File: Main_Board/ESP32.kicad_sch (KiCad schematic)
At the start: 25 parts, among them J1 RESET, J2 MAIN_UART, Q1 2N7002, U1 W25Q128JVS, U2 ESP32-S3-MINI-1U

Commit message: memory fix + piro
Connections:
- net CLK_SPI2: now also U2.18 (IO14); no longer U2.17 (IO13)
- net IO0 / MOSI: now also U2.17 (IO13); no longer U2.18 (IO14)
- net IO2 / WP: now also U2.16 (IO12); no longer U2.19 (IO15)
- net IO3 / HOLD: no longer U1.7 (~{HOLD}/~{RESET}/IO_{3}), U2.16 (IO12)
- new net: U1.7 (~{HOLD}/~{RESET}/IO_{3}), U2.19 (IO15)
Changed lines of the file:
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@@
+	(wire
+		(pts
+			(xy 105.41 138.43) (xy 111.76 138.43)
+		)
+		(stroke
+			(width 0)
+			(type default)
+		)
+	)
 	(wire
 		(pts
@@
 	(wire
 		(pts
-			(xy 71.12 134.62) (xy 125.73 134.62)
+			(xy 110.49 142.24) (xy 125.73 142.24)
 		)
 		(stroke
@@
 	(wire
 		(pts
-			(xy 71.12 137.16) (xy 125.73 137.16)
+			(xy 71.12 142.24) (xy 109.22 142.24)
 		)
 		(stroke
@@
 	(wire
 		(pts
-			(xy 71.12 142.24) (xy 125.73 142.24)
-		)
-		(stroke
-			(width 0)
-			(type default)
-		)
-	)
-	(wire
-		(pts
 			(xy 71.12 132.08) (xy 125.73 132.08)
 		)
@@
 	(wire
 		(pts
+			(xy 106.68 139.7) (xy 125.73 139.7)
+		)
+		(stroke
+			(width 0)
+			(type default)
+		)
+	)
+	(wire
+		(pts
 			(xy 193.04 93.98) (xy 193.04 101.6)
 		)
@@
 	(wire
 		(pts
+			(xy 111.76 137.16) (xy 125.73 137.16)
+		)
+		(stroke
+			(width 0)
+			(type default)
+		)
+	)
+	(wire
+		(pts
 			(xy 233.68 96.52) (xy 233.68 86.36)
 		)
@@
 	(wire
 		(pts
+			(xy 106.68 137.16) (xy 106.68 139.7)
+		)
+		(stroke
+			(width 0)
+			(type default)
+		)
+	)
+	(wire
+		(pts
 			(xy 200.66 88.9) (xy 201.93 88.9)
 		)
@@
 	(wire
 		(pts
-			(xy 71.12 139.7) (xy 125.73 139.7)
-		)
-		(stroke
-			(width 0)
-			(type default)
-		)
-	)
-	(wire
-		(pts
 			(xy 106.68 116.84) (xy 110.49 116.84)
 		)
@@
 	(wire
 		(pts
+			(xy 109.22 134.62) (xy 125.73 134.62)
+		)
+		(stroke
+			(width 0)
+			(type default)
+		)
+	)
+	(wire
+		(pts
 			(xy 119.38 147.32) (xy 125.73 147.32)
 		)
@@
 	(wire
 		(pts
+			(xy 110.49 140.97) (xy 110.49 142.24)
+		)
+		(stroke
+			(width 0)
+			(type default)
+		)
+	)
+	(wire
+		(pts
 			(xy 114.3 99.06) (xy 125.73 99.06)
 		)
@@
 	(wire
 		(pts
+			(xy 83.82 140.97) (xy 110.49 140.97)
+		)
+		(stroke
+			(width 0)
+			(type default)
+		)
+	)
+	(wire
+		(pts
 			(xy 104.14 149.86) (xy 111.76 149.86)
 		)
@@
 	(wire
 		(pts
+			(xy 83.82 134.62) (xy 83.82 140.97)
+		)
+		(stroke
+			(width 0)
+			(type default)
+		)
+	)
+	(wire
+		(pts
+			(xy 71.12 134.62) (xy 83.82 134.62)
+		)
+		(stroke
+			(width 0)
+			(type default)
+		)
+	)
+	(wire
+		(pts
 			(xy 104.14 147.32) (xy 111.76 147.32)
 		)
@@
 	(wire
 		(pts
+			(xy 111.76 137.16) (xy 111.76 138.43)
+		)
+		(stroke
+			(width 0)
+			(type default)
+		)
+	)
+	(wire
+		(pts
 			(xy 54.61 34.29) (xy 54.61 33.02)
 		)
@@
 	(wire
 		(pts
+			(xy 71.12 139.7) (xy 105.41 139.7)
+		)
+		(stroke
+			(width 0)
+			(type default)
+		)
+	)
+	(wire
+		(pts
 			(xy 106.68 119.38) (xy 110.49 119.38)
 		)
@@
 	(wire
 		(pts
+			(xy 105.41 138.43) (xy 105.41 139.7)
+		)
+		(stroke
+			(width 0)
+			(type default)
+		)
+	)
+	(wire
+		(pts
+			(xy 109.22 142.24) (xy 109.22 134.62)
+		)
+		(stroke
+			(width 0)
+			(type default)
+		)
+	)
+	(wire
+		(pts
 			(xy 60.96 123.19) (xy 60.96 124.46)
 		)
@@
 		)
 		(stroke
+			(width 0)
+			(type default)
+		)
+	)
+	(wire
+		(pts
+			(xy 71.12 137.16) (xy 106.68 137.16)
+		)
+		(stroke

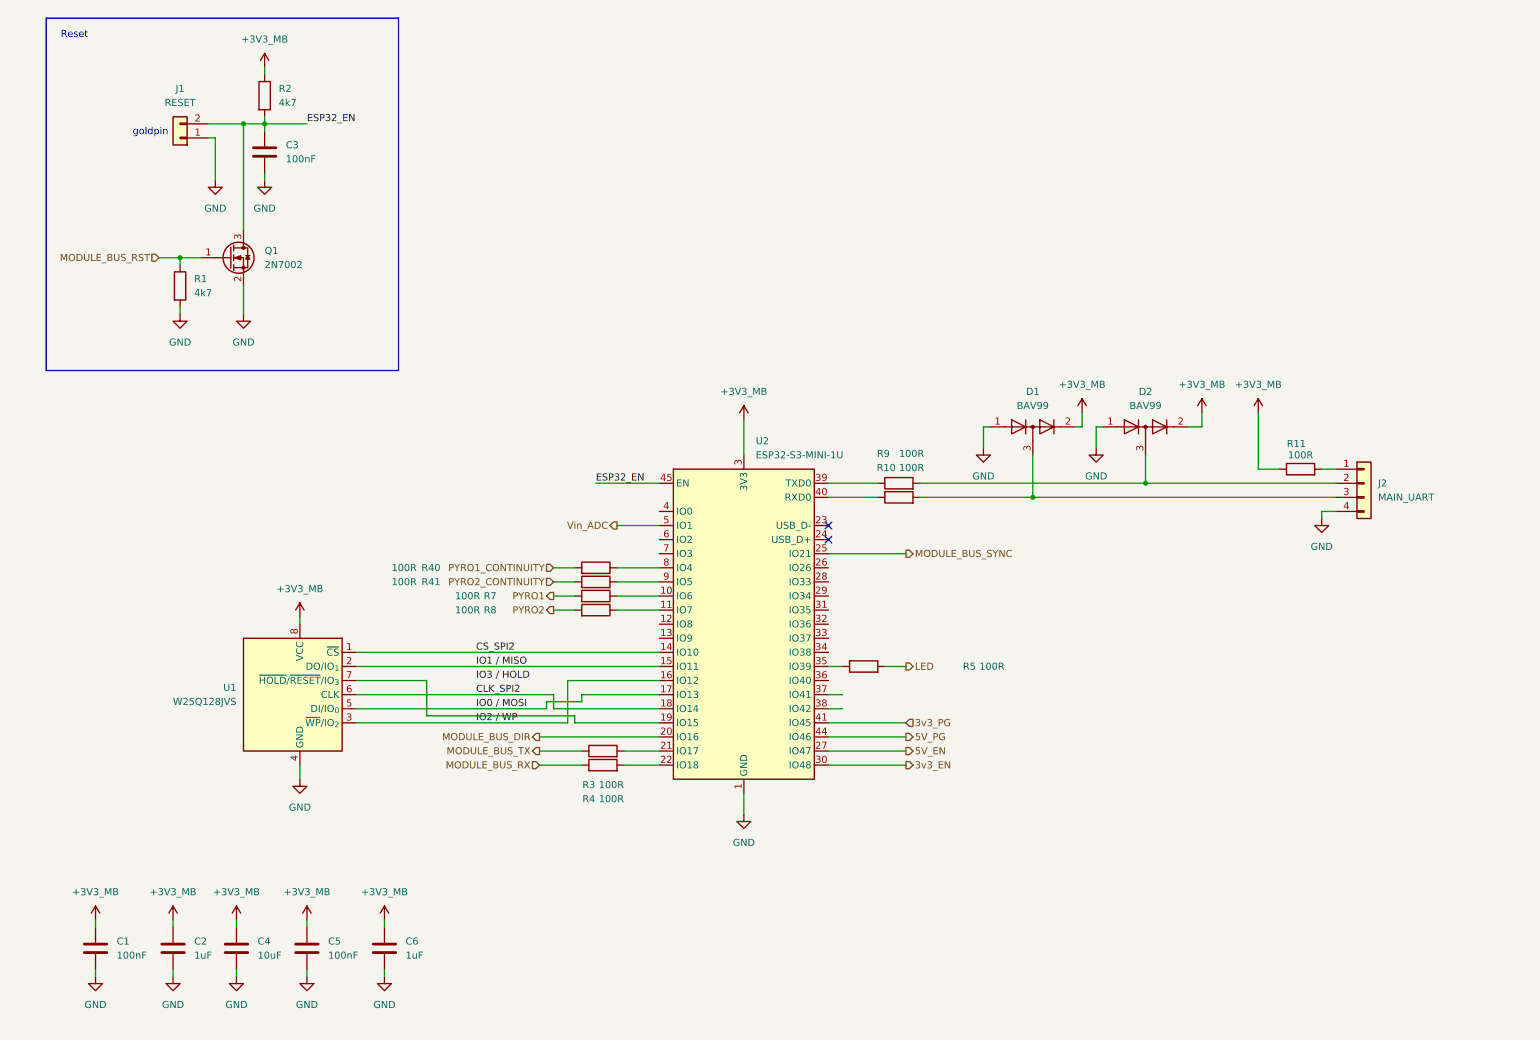
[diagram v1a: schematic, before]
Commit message: Schematic cleanup, ALED footprint + 3D + sch
+ layout and routing
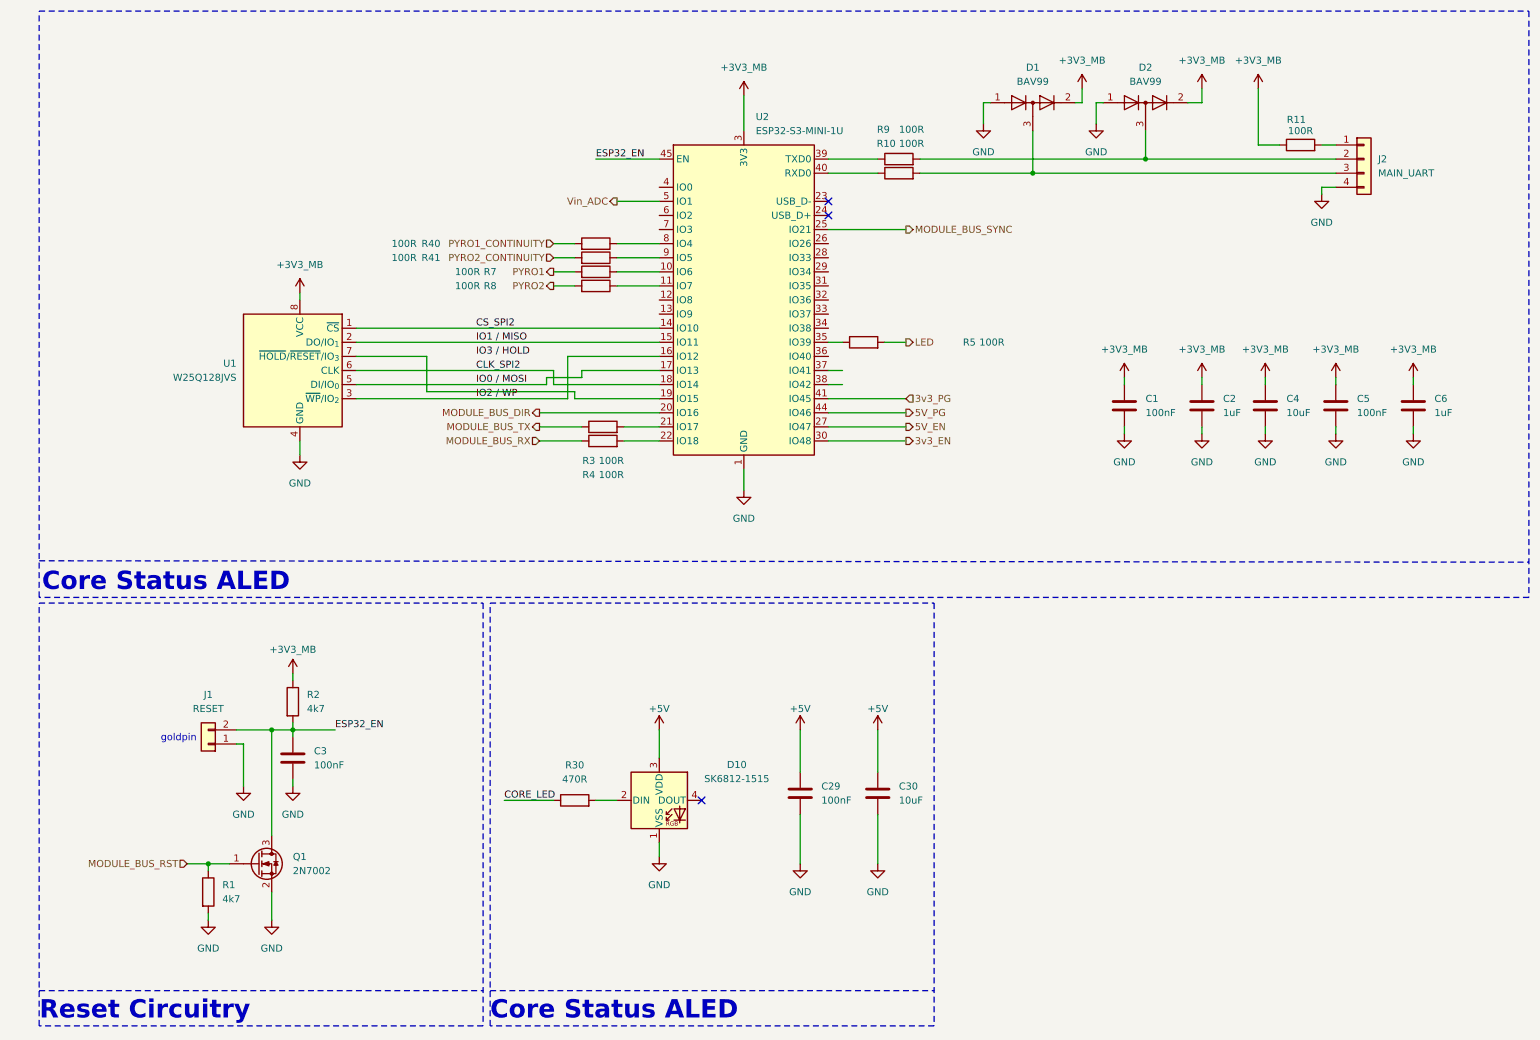
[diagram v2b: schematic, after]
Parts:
- added C29: 100nF, Capacitor_SMD:C_0603_1608Metric, symbol Device:C
- added C30: 10uF, Capacitor_SMD:C_0603_1608Metric, symbol Device:C
- added D10: SK6812-1515, sk6805-1515:sk68015-1515, symbol LED:SK6812
- added R30: 470R, Resistor_SMD:R_0603_1608Metric, symbol Device:R
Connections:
- net GND: now also C29.2, C30.2, D10.1 (VSS)
- new net: D10.2 (DIN), R30.2
- new net +5V: C29.1, C30.1, D10.3 (VDD)
- new net CORE_LED: R30.1
- no-connect marks 2 -> 3
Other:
- note added: "Core Status ALED"
- note added: "Reset Circuitry"
- note removed: "Reset"
- moved on the sheet: C1, C2, C3, C4, C5, C6, D1, D2, J1, J2, Q1, R1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

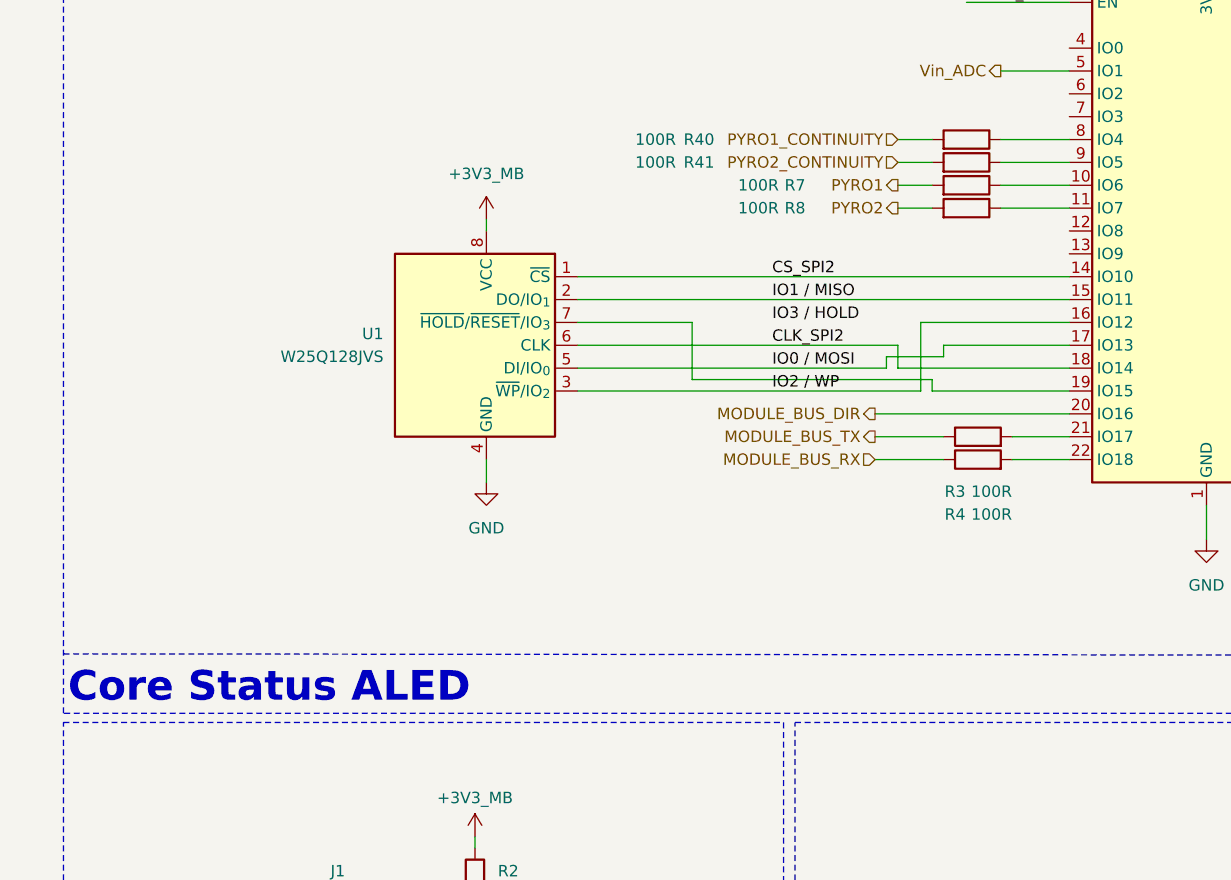
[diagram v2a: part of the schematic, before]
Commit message: Unspaghettify flash schematic
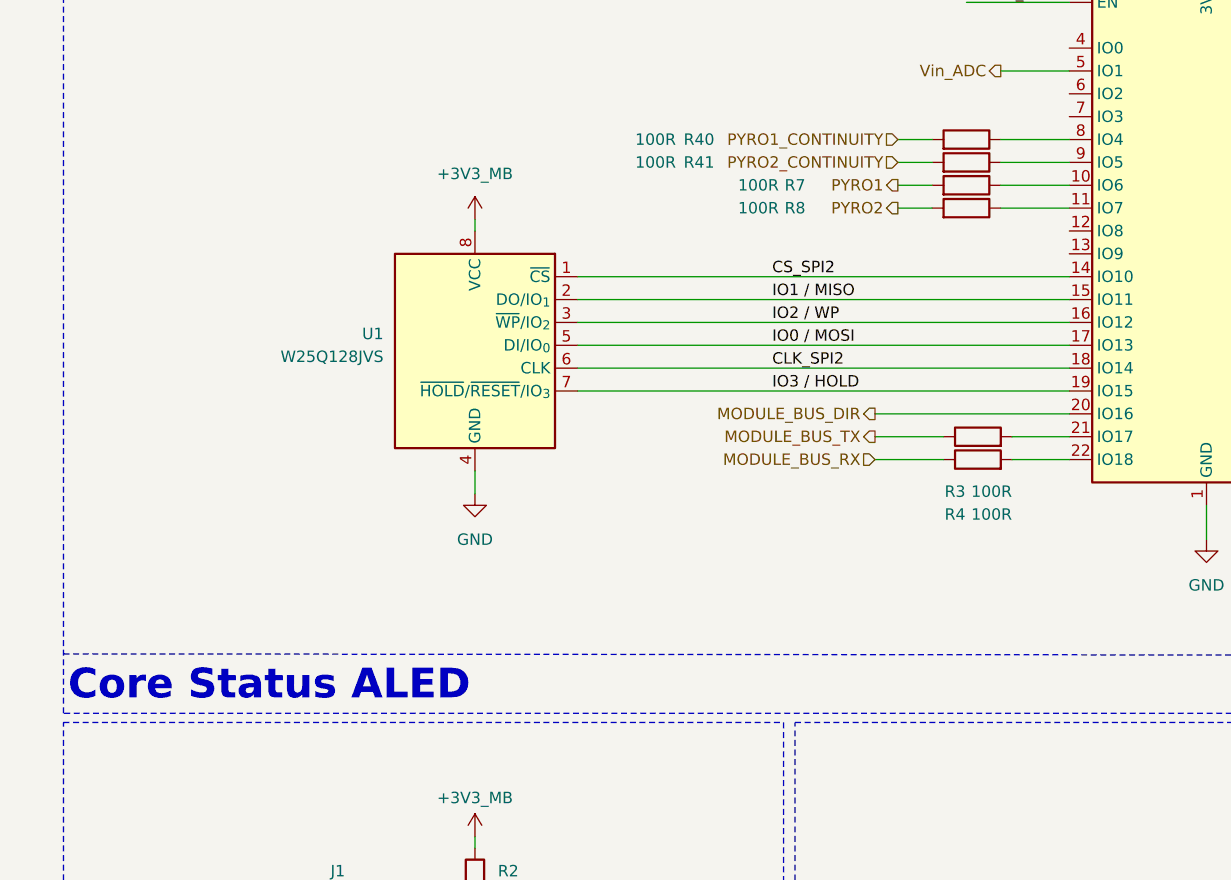
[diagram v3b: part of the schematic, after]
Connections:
- net IO3 / HOLD: now also U1.7 (~{HOLD}/~{RESET}/IO_{3}), U2.19 (IO15)
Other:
- moved on the sheet: U1
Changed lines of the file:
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@@
 	(text "Core Status ALED"
 		(exclude_from_sim no)
-		(at 36.83 116.84 0)
+		(at 36.83 116.586 0)
 		(effects
 			(font
@@
 	(wire
 		(pts
-			(xy 105.41 80.01) (xy 111.76 80.01)
-		)
-		(stroke
-			(width 0)
-			(type default)
-		)
-	)
-	(wire
-		(pts
 			(xy 261.62 80.01) (xy 261.62 81.28)
 		)
@@
 	(wire
 		(pts
-			(xy 110.49 83.82) (xy 125.73 83.82)
-		)
-		(stroke
-			(width 0)
-			(type default)
-		)
-	)
-	(wire
-		(pts
 			(xy 223.52 30.48) (xy 223.52 27.94)
 		)
@@
 	(wire
 		(pts
-			(xy 71.12 83.82) (xy 109.22 83.82)
+			(xy 71.12 83.82) (xy 125.73 83.82)
 		)
 		(stroke
@@
 	(wire
 		(pts
-			(xy 106.68 81.28) (xy 125.73 81.28)
-		)
-		(stroke
-			(width 0)
-			(type default)
-		)
-	)
-	(wire
-		(pts
 			(xy 193.04 35.56) (xy 193.04 43.18)
 		)
@@
 	(wire
 		(pts
-			(xy 111.76 78.74) (xy 125.73 78.74)
-		)
-		(stroke
-			(width 0)
-			(type default)
-		)
-	)
-	(wire
-		(pts
 			(xy 233.68 38.1) (xy 233.68 27.94)
 		)
@@
 	(wire
 		(pts
-			(xy 106.68 78.74) (xy 106.68 81.28)
-		)
-		(stroke
-			(width 0)
-			(type default)
-		)
-	)
-	(wire
-		(pts
 			(xy 200.66 30.48) (xy 201.93 30.48)
 		)
@@
 	(wire
 		(pts
-			(xy 60.96 91.44) (xy 60.96 93.98)
+			(xy 59.69 92.71) (xy 59.69 95.25)
 		)
 		(stroke
@@
 	(wire
 		(pts
+			(xy 71.12 78.74) (xy 125.73 78.74)
+		)
+		(stroke
+			(width 0)
+			(type default)
+		)
+	)
+	(wire
+		(pts
 			(xy 106.68 58.42) (xy 110.49 58.42)
 		)
@@
 	(wire
 		(pts
-			(xy 109.22 76.2) (xy 125.73 76.2)
-		)
-		(stroke
-			(width 0)
-			(type default)
-		)
-	)
-	(wire
-		(pts
 			(xy 119.38 88.9) (xy 125.73 88.9)
 		)
@@
 	(wire
 		(pts
-			(xy 110.49 82.55) (xy 110.49 83.82)
+			(xy 71.12 81.28) (xy 125.73 81.28)
 		)
 		(stroke
@@
 	(wire
 		(pts
-			(xy 83.82 82.55) (xy 110.49 82.55)
-		)
-		(stroke
-			(width 0)
-			(type default)
-		)
-	)
-	(wire
-		(pts
 			(xy 104.14 91.44) (xy 111.76 91.44)
 		)
@@
 	(wire
 		(pts
-			(xy 83.82 76.2) (xy 83.82 82.55)
-		)
-		(stroke
-			(width 0)
-			(type default)
-		)
-	)
-	(wire
-		(pts
-			(xy 71.12 76.2) (xy 83.82 76.2)
-		)
-		(stroke
-			(width 0)
-			(type default)
-		)
-	)
-	(wire
-		(pts
 			(xy 104.14 88.9) (xy 111.76 88.9)
 		)
@@
 	(wire
 		(pts
-			(xy 111.76 78.74) (xy 111.76 80.01)
-		)
-		(stroke
-			(width 0)
-			(type default)
-		)
-	)
-	(wire
-		(pts
 			(xy 59.69 143.51) (xy 59.69 142.24)
 		)
@@
 	(wire
 		(pts
-			(xy 71.12 81.28) (xy 105.41 81.28)
+			(xy 71.12 76.2) (xy 125.73 76.2)
 		)
 		(stroke
@@
 	(wire
 		(pts
-			(xy 105.41 80.01) (xy 105.41 81.28)
-		)
-		(stroke
-			(width 0)
-			(type default)
-		)
-	)
-	(wire
-		(pts
-			(xy 109.22 83.82) (xy 109.22 76.2)
-		)
-		(stroke
-			(width 0)
-			(type default)
-		)
-	)
-	(wire
-		(pts
-			(xy 60.96 64.77) (xy 60.96 66.04)
+			(xy 59.69 64.77) (xy 59.69 66.04)
 		)
 		(stroke
@@
 		)
 	)
-	(wire
-		(pts
-			(xy 71.12 78.74) (xy 106.68 78.74)
-		)
-		(stroke
-			(width 0)
-			(type default)
-		)
-	)
 	(label "IO2 {slash} WP"
-		(at 92.71 83.82 0)
+		(at 92.71 76.2 0)
 		(effects
 			(font
@@
 	)
 	(label "IO0 {slash} MOSI"
-		(at 92.71 81.28 0)
+		(at 92.71 78.74 0)
 		(effects
 			(font
@@
 	)
 	(label "IO3 {slash} HOLD"
-		(at 92.71 76.2 0)
+		(at 92.71 83.82 0)
 		(effects
 			(font
@@
 	)
 	(label "CLK_SPI2"
-		(at 92.71 78.74 0)
+		(at 92.71 81.28 0)
 		(effects
 			(font
@@
 	(symbol
 		(lib_id "power:+3V3")
-		(at 60.96 64.77 0)
+		(at 59.69 64.77 0)
 		(unit 1)
 		(body_style 1)
@@
 		(fields_autoplaced yes)
 		(property "Reference" "#PWR014"
-			(at 60.96 68.58 0)
+			(at 59.69 68.58 0)
 			(hide yes)
 			(show_name no)
@@
 		)
 		(property "Value" "+3V3_MB"
-			(at 60.96 59.69 0)
+			(at 59.69 59.69 0)
 			(show_name no)
 			(do_not_autoplace no)
@@
 		)
 		(property "Footprint" ""
-			(at 60.96 64.77 0)
+			(at 59.69 64.77 0)
 			(hide yes)
 			(show_name no)
@@
 		)
 		(property "Datasheet" ""
-			(at 60.96 64.77 0)
+			(at 59.69 64.77 0)
 			(hide yes)
 			(show_name no)
@@
 		)
 		(property "Description" "Power symbol creates a global label with name \"+3V3\""
-			(at 60.96 64.77 0)
+			(at 59.69 64.77 0)
 			(hide yes)
 			(show_name no)
@@
 	(symbol
 		(lib_id "power:GND")
-		(at 60.96 93.98 0)
+		(at 59.69 95.25 0)
 		(unit 1)
 		(body_style 1)
@@
 		(fields_autoplaced yes)
 		(property "Reference" "#PWR015"
-			(at 60.96 100.33 0)
+			(at 59.69 101.6 0)
 			(hide yes)
 			(show_name no)
@@
 		)
 		(property "Value" "GND"
-			(at 60.96 99.06 0)
+			(at 59.69 100.33 0)
 			(show_name no)
 			(do_not_autoplace no)
@@
 		)
 		(property "Footprint" ""
-			(at 60.96 93.98 0)
+			(at 59.69 95.25 0)
 			(hide yes)
 			(show_name no)
@@
 		)
 		(property "Datasheet" ""
-			(at 60.96 93.98 0)
+			(at 59.69 95.25 0)
 			(hide yes)
 			(show_name no)
@@
 		)
 		(property "Description" "Power symbol creates a global label with name \"GND\" , ground"
-			(at 60.96 93.98 0)
-			(hide yes)
-			(show_name no)
+			(at 59.69 95.25 0)
+			(hide yes)
+			(show_name no)

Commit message: ALED
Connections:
- net LED is gone; now on net CORE_LED: R5.2
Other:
- moved on the sheet: C29, C30, D10, R30
